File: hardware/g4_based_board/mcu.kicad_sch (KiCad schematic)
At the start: 17 parts, among them SW1 RESET, SW2 SW_SPDT, U1 STM32G431R6Tx, Y1 12MHz, 20pF

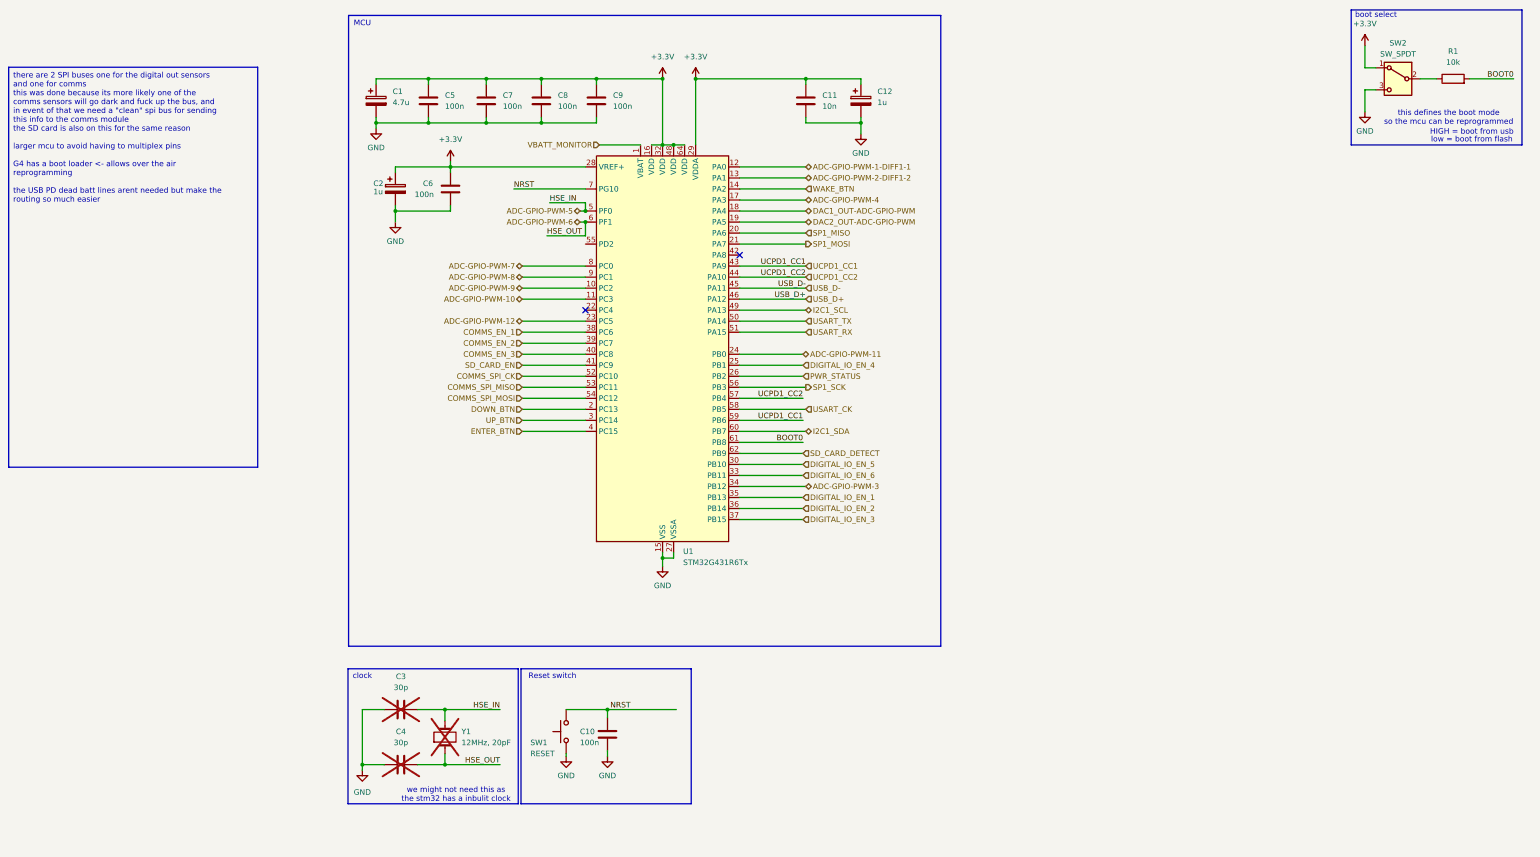
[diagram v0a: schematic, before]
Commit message: minor addtion and swd header added and usart removed
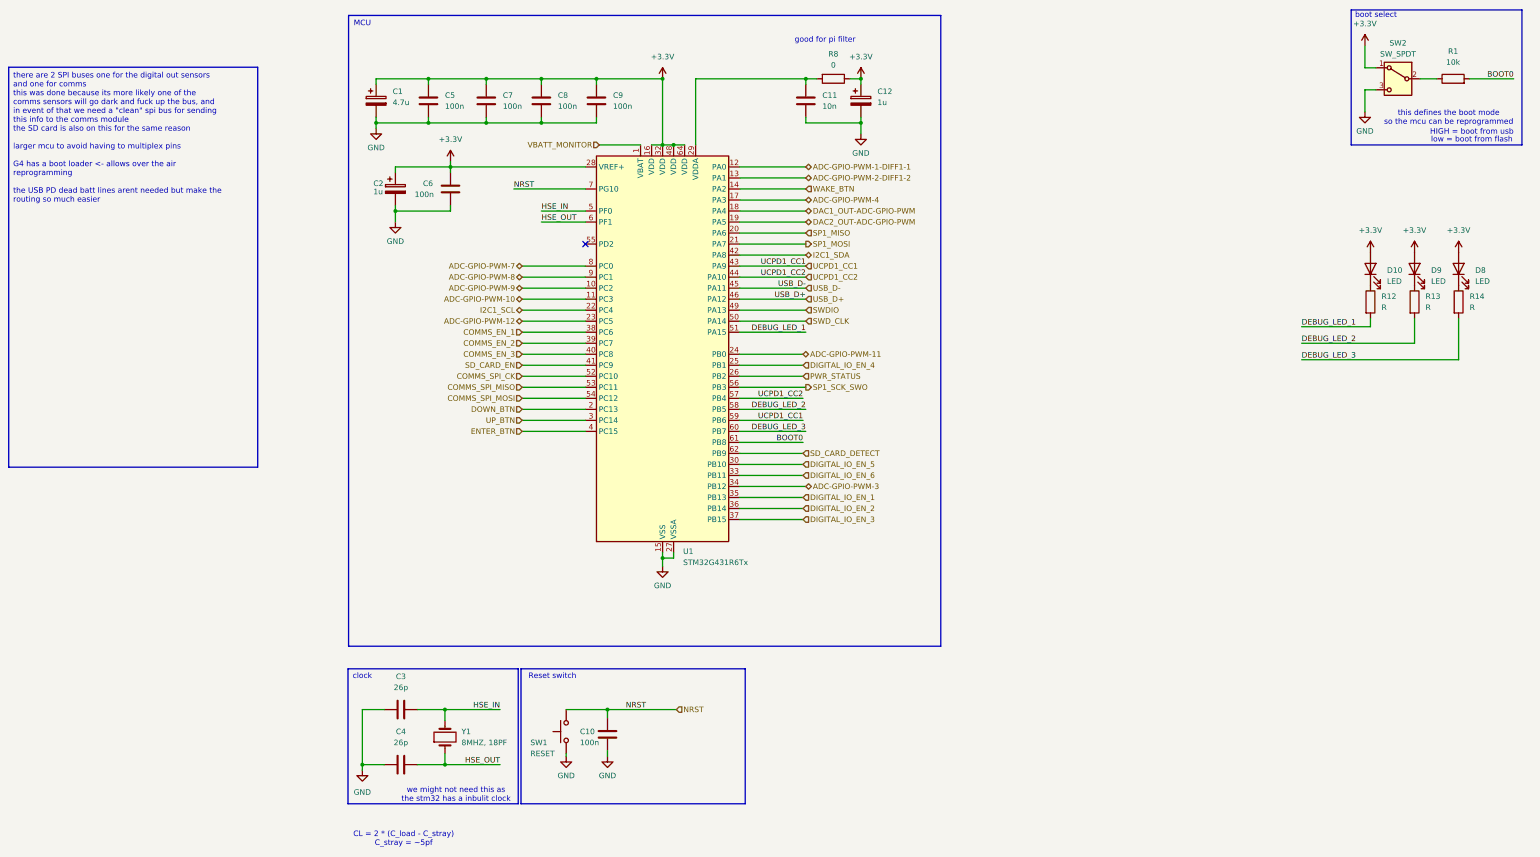
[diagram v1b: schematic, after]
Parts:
- added D10, D8, D9: LED, LED_SMD:LED_0603_1608Metric, symbol Device:LED
- added R12, R13, R14: R, Resistor_SMD:R_0603_1608Metric_Pad0.98x0.95mm_HandSolder, symbol Device:R
- added R8: 0, Resistor_SMD:R_0603_1608Metric, symbol Device:R
- C3, C4: value 30p -> 26p; now fitted
- Y1: value 12MHz, 20pF -> 8MHZ, 18PF; footprint Crystal:Crystal_HC49-U_Vertical -> Crystal:Crystal_SMD_TXC_7A-2Pin_5x3.2mm; now fitted
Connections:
- net +3.3V: now also D10.2 (A), D8.2 (A), D9.2 (A), R8.1; no longer C11.1, U1.29 (VDDA)
- net I2C1_SCL: now also U1.22 (PC4); no longer U1.49 (PA13)
- net I2C1_SDA: now also U1.42 (PA8); no longer U1.60 (PB7)
- net ADC-GPIO-PWM-5 renamed HSE_IN
- net ADC-GPIO-PWM-6 renamed HSE_OUT
- net SP1_SCK renamed SP1_SCK_SWO
- net USART_CK renamed DEBUG_LED_2
- net DEBUG_LED_2: now also R13.2
- net USART_RX renamed DEBUG_LED_1
- net DEBUG_LED_1: now also R12.2
- net USART_TX renamed SWD_CLK
- new net: D9.1 (K), R13.1
- new net: D8.1 (K), R14.1
- new net: C11.1, R8.2, U1.29 (VDDA)
- new net: D10.1 (K), R12.1
- new net DEBUG_LED_3: R14.2, U1.60 (PB7)
- new net SWDIO: U1.49 (PA13)
- no-connect marks 2 -> 1
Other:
- note added: "CL = 2 * (C_load - C_stray) C_stray = ~5pf"
- note added: "good for pi filter"

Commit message: swapped assignment to differnt pins
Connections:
- net +3.3V: no longer C1.1
- net COMMS_EN_1: now also U1.2 (PC13); no longer U1.38 (PC6)
- net COMMS_EN_2: now also U1.3 (PC14); no longer U1.39 (PC7)
- net COMMS_EN_3: now also U1.4 (PC15); no longer U1.40 (PC8)
- net DEBUG_LED_1: now also U1.55 (PD2); no longer U1.51 (PA15)
- net DOWN_BTN: now also U1.38 (PC6); no longer U1.2 (PC13)
- net ENTER_BTN: now also U1.40 (PC8); no longer U1.4 (PC15)
- net PWR_STATUS: now also U1.41 (PC9); no longer U1.26 (PB2)
- net SD_CARD_EN: now also U1.51 (PA15); no longer U1.41 (PC9)
- net UP_BTN: now also U1.39 (PC7); no longer U1.3 (PC14)
- net VBATT_MONITOR: now also C1.1
- net DIGITAL_IO_EN_4 renamed PWM_2
- new net PWM_1: U1.26 (PB2)
- no-connect marks 1 -> 0
